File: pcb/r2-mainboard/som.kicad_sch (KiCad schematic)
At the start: 14 parts, among them J21 MICRO_SD(TFC-WPAPR-08), J26 BTH-060-01-L-D-A-K-TR, J27 BTH-060-01-L-D-A-K-TR, X2 PCM-071

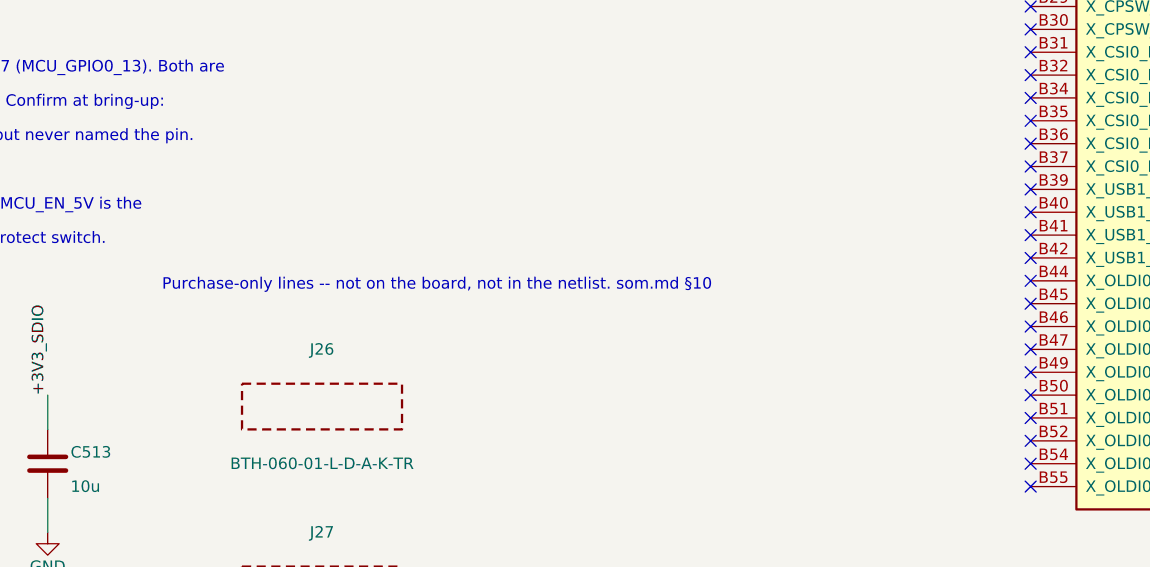
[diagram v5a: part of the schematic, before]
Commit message: R2: make the board arrive with the connectors already soldered
The question "why are they not on the board?" found a real hole, and my
previous commit had only half-fixed it. Making J26/J27 purchase-only put
the parts on the order and left the board unassemblable, because a part
that is not on the board is not in the position file either.

A CPL has one row per reference. X2 alone produces a single placement at a
single centroid, for a footprint that two separate parts occupy 22.4 mm
apart and 4.8 mm staggered -- there is no part covering all 240 pads. And
JLCPCB rejects a CPL designator with no BOM line, which X2 is. A board
ordered that way comes back with 240 bare pads.

So the two jobs are split. The pads stay under X2, which is now marked
exclude_from_pos_files. J26/J27 get r2:BTH-060-01-L-D-A-K_AssemblyOnly --
a body outline with no pads -- so each receptacle gets its own CPL row and
its own BOM match against C3646540. The assembler places a real part at
each real centroid; the paste and copper it lands on come from X2, which
they never need to know about.

Nothing in KiCad ties the three footprints together, so the relationship is
asserted rather than remembered: check_pcb_connectors.py requires
J26 = X2 + (-11.200, +2.400) and J27 = X2 + (+11.200, -2.400), plus same
side, same rotation, no pads on the markers, and the exclude_from_pos_files
split intact. Tested against three synthetic boards -- passes the good one,
catches a 2 mm nudge and a missing exclusion. That is a stronger guarantee
than the single footprint gave, which was unbreakable but also unverifiable.

517 nets before and after, ERC unchanged at 32. Two things still to confirm
with JLCPCB before the first order, both in som.md 10.0: whether their DFM
review accepts a no-pad designator, and the CPL rotation convention for
these connectors.

Co-Authored-By: Claude Opus 5 <noreply@anthropic.com>
Claude-Session: https://claude.ai/code/session_01MnesETWABbVdbcVnCKfKVs
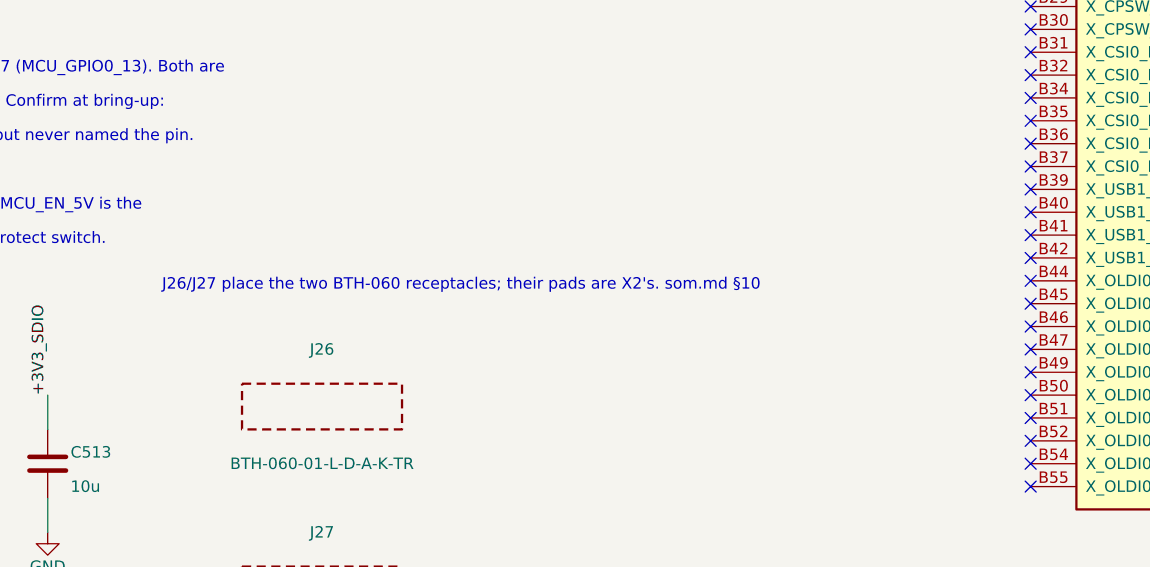
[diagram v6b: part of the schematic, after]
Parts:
- J26: footprint (none) -> r2:BTH-060-01-L-D-A-K_AssemblyOnly; BOM Comments Board-side receptacle for the PCM-071, 2 per board. Soldere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 -> Board-side receptacle for the PCM-071, 2 per board, SOLDERE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
- J27: footprint (none) -> r2:BTH-060-01-L-D-A-K_AssemblyOnly; BOM Comments The second of the two. See J26. -> The second of the two. Place at X2 + (+11.200, -2.400). See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
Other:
- note added: "J26/J27 place the two BTH-060 receptacles; their pads are X2's. som.md §10"
- note removed: "Purchase-only lines -- not on the board, not in the netlist. som.md §10"
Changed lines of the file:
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@@
 		)
 	)
-	(text "Purchase-only lines -- not on the board, not in the netlist. som.md §10"
+	(text "J26/J27 place the two BTH-060 receptacles; their pads are X2's. som.md §10"
 		(exclude_from_sim no)
 		(at 218.44 190.5 0)
@@
 		(exclude_from_sim no)
 		(in_bom yes)
-		(on_board no)
+		(on_board yes)
 		(dnp no)
 		(property "Reference" "J26"
@@
 			)
 		)
-		(property "Footprint" ""
+		(property "Footprint" "r2:BTH-060-01-L-D-A-K_AssemblyOnly"
 			(at 236.22 203.2 0)
 			(hide yes)
@@
 			)
 		)
-		(property "BOM Comments" "Board-side receptacle for the PCM-071, 2 per board. Soldered to r2:PCM-071_2xBTH-060-01-L-D-A-K, which carries both patterns in one footprint -- so this symbol is on_board=no and exists only to put the part on the order. LCSC stock was 60 on 2026-08-20; C3644612 is the same connector without the -K option. som.md section 10."
+		(property "BOM Comments" "Board-side receptacle for the PCM-071, 2 per board, SOLDERED BY THE ASSEMBLER. Its pads are in r2:PCM-071_2xBTH-060-01-L-D-A-K under X2; this reference carries the CPL row and the BOM match, and its own footprint has no pads. Place at X2 + (-11.200, +2.400) -- checked by tools/check_pcb_connectors.py. LCSC stock was 60 on 2026-08-20; C3644612 is the same connector without the -K option. som.md section 10."
 			(at 236.22 203.2 0)
 			(hide yes)
@@
 		(exclude_from_sim no)
 		(in_bom yes)
-		(on_board no)
+		(on_board yes)
 		(dnp no)
 		(property "Reference" "J27"
@@
 			)
 		)
-		(property "Footprint" ""
+		(property "Footprint" "r2:BTH-060-01-L-D-A-K_AssemblyOnly"
 			(at 236.22 223.52 0)
 			(hide yes)
@@
 			)
 		)
-		(property "BOM Comments" "The second of the two. See J26."
+		(property "BOM Comments" "The second of the two. Place at X2 + (+11.200, -2.400). See J26."
 			(at 236.22 223.52 0)
 			(hide yes)

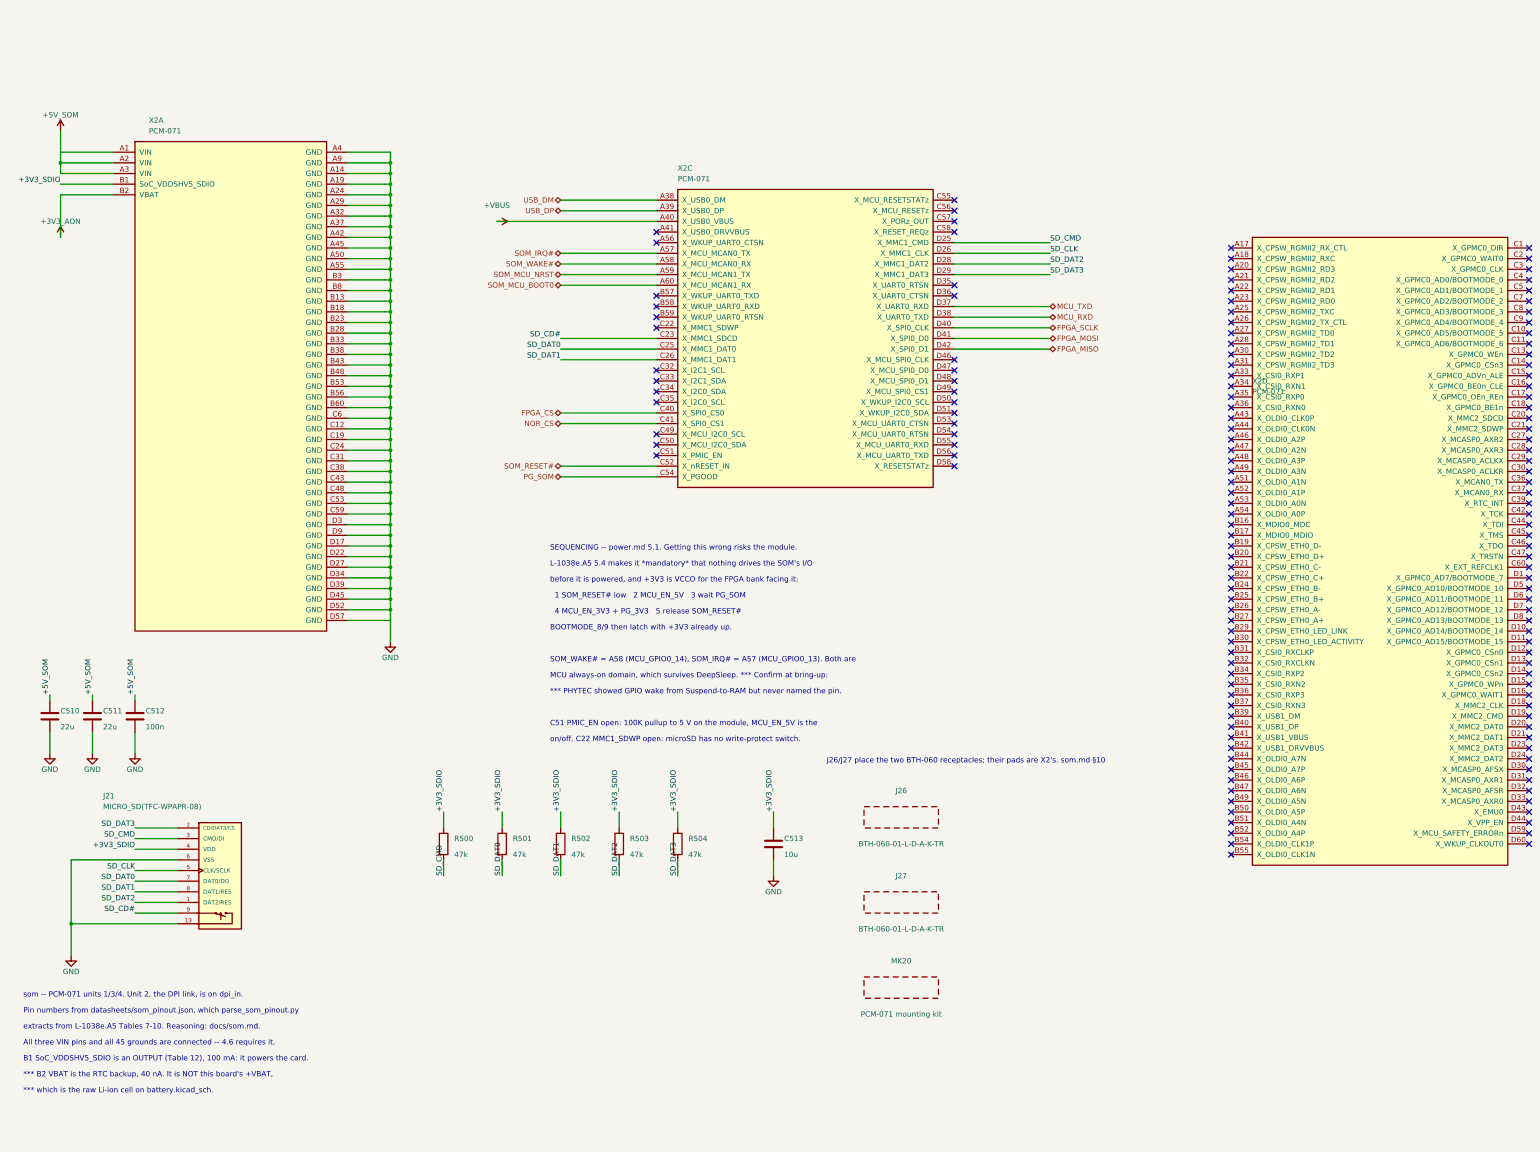
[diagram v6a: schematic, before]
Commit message: R2: the SoM is now two connectors, which is what the board has
The owner's call, and the right one: "I would rather have the two BTH
connectors and connect all signals/lines etc. to those two instead of the
A,B,... split. Then routing it later would also make more sense for me."
Clever loses to clear -- and the clever version could not be assembled
anyway, because a position file has one row per reference and there is no
single part covering 240 pads.

J26 carries the module's A and B columns, J27 its C and D, 120 pins each.
X2 survives as the module: outline and the two M2.5 holes, no pads, no
nets, excluded from the position file because it is fitted by hand. Three
footprints replace the one. Six unit boxes on som instead of three, two on
dpi_in instead of one; the root hierarchy is untouched.

What made this safe is that it is a repartition, not a renumber. Pin
numbers stay A1-A60 / B1-B60 / C1-C60 / D1-D60 exactly as L-1038e.A5
Tables 7-10 print them -- not Samtec's 1-120 alternating numbering -- and
the footprints name their pads the same way. Names, numbers and electrical
types are untouched; only which symbol a pin belongs to changes.

The acceptance test was exact: the netlist must be identical except every
X2.<pin> becomes J26.<pin> or J27.<pin> by row. It is -- 517 nets, 270
named nets with identical membership, 247 unconnected pins. ERC unchanged
at 32. Both sheets rendered and checked; two text collisions found that way
and fixed by deriving ref/val offsets from each box's own height.

check_pcb_connectors.py keeps the geometry guarantee the single footprint
used to give structurally, and now verifies it instead: J26 = X2 +
(-11.200, -2.400), J27 = X2 + (+11.200, +2.400), same side, same rotation,
122 pads each against the module's 2.

Two bugs fixed on the way, neither about the restructure. gen_som.py could
not find som_pinout.json -- it hardcoded datasheets/<name>, which broke in
the 2026-08-19 reorganisation; 058e9b9 fixed three tools and missed this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
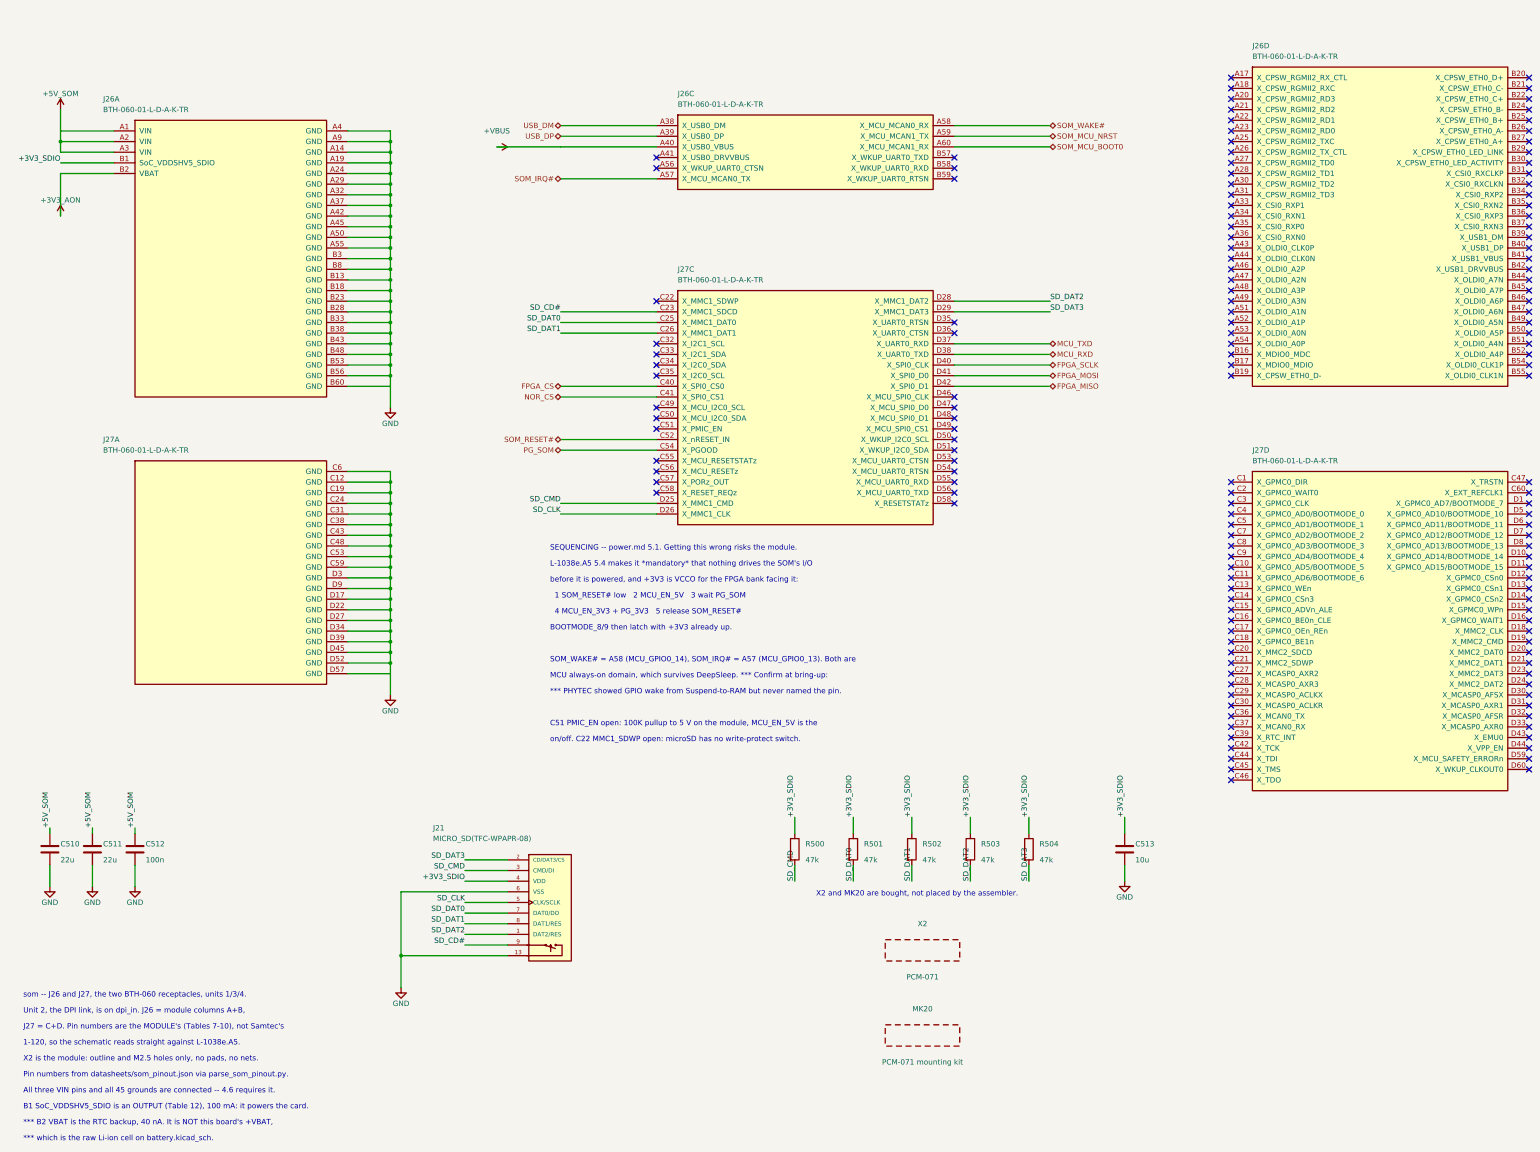
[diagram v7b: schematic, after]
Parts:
- removed J26, J27: BTH-060-01-L-D-A-K-TR, r2:BTH-060-01-L-D-A-K_AssemblyOnly, symbol r2:BOM_ITEM
- removed X2: PCM-071, r2:PCM-071_2xBTH-060-01-L-D-A-K, symbol r2:PCM-071
- added J26: BTH-060-01-L-D-A-K-TR, r2:BTH-060-01-L-D-A-K_AB, symbol r2:BTH-060_AB
- added J27: BTH-060-01-L-D-A-K-TR, r2:BTH-060-01-L-D-A-K_CD, symbol r2:BTH-060_CD
- added X2: PCM-071, r2:PCM-071_Module, symbol r2:BOM_ITEM
- MK20: BOM Comments PHYTEC's own recommendation, L-1038e.A5 section 4.3. Not optional: the standoffs set the 5 mm stacking height the BTH-060 pair is specified for, so without them the connector solder joints carry the module's mechanical load. Holes are in the footprint at (2.8, 2.8) and (29.2, 40.2) relative to the module outline. -> PHYTEC's own recommendation, L-1038e.A5 section 4.3. Not optional: the standoffs set the 5 mm stacking height the BTH-060 pair is specified for, so without them the connector solder joints carry the module's mechanical load.
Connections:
- net +3V3_AON: now also J26.B2 (VBAT)
- net +3V3_SDIO: now also J26.B1 (SoC_VDDSHV5_SDIO)
- net +5V_SOM: now also J26.A1 (VIN), J26.A2 (VIN), J26.A3 (VIN)
- net +VBUS: now also J26.A40 (X_USB0_VBUS)
- net FPGA_CS: now also J27.C40 (X_SPI0_CS0)
- net FPGA_MISO: now also J27.D42 (X_SPI0_D1)
- net FPGA_MOSI: now also J27.D41 (X_SPI0_D0)
- net FPGA_SCLK: now also J27.D40 (X_SPI0_CLK)
- net GND: now also J26.A14 (GND), J26.A19 (GND), J26.A24 (GND), J26.A29 (GND), J26.A32 (GND), J26.A37 (GND), J26.A4 (GND), J26.A42 (GND), J26.A45 (GND), J26.A50 (GND), J26.A55 (GND), J26.A9 (GND), J26.B13 (GND), J26.B18 (GND), J26.B23 (GND), J26.B28 (GND), J26.B3 (GND), J26.B33 (GND), J26.B38 (GND), J26.B43 (GND), J26.B48 (GND), J26.B53 (GND), J26.B56 (GND), J26.B60 (GND), J26.B8 (GND), J27.C12 (GND), J27.C19 (GND), J27.C24 (GND), J27.C31 (GND), J27.C38 (GND), J27.C43 (GND), J27.C48 (GND), J27.C53 (GND), J27.C59 (GND), J27.C6 (GND), J27.D17 (GND), J27.D22 (GND), J27.D27 (GND), J27.D3 (GND), J27.D34 (GND), J27.D39 (GND), J27.D45 (GND), J27.D52 (GND), J27.D57 (GND), J27.D9 (GND)
- net MCU_RXD: now also J27.D38 (X_UART0_TXD)
- net MCU_TXD: now also J27.D37 (X_UART0_RXD)
- net NOR_CS: now also J27.C41 (X_SPI0_CS1)
- net PG_SOM: now also J27.C54 (X_PGOOD)
- net SD_CD#: now also J27.C23 (X_MMC1_SDCD)
- net SD_CLK: now also J27.D26 (X_MMC1_CLK)
- net SD_CMD: now also J27.D25 (X_MMC1_CMD)
- net SD_DAT0: now also J27.C25 (X_MMC1_DAT0)
- net SD_DAT1: now also J27.C26 (X_MMC1_DAT1)
- net SD_DAT2: now also J27.D28 (X_MMC1_DAT2)
- net SD_DAT3: now also J27.D29 (X_MMC1_DAT3)
- net SOM_IRQ#: now also J26.A57 (X_MCU_MCAN0_TX)
- net SOM_MCU_BOOT0: now also J26.A60 (X_MCU_MCAN1_RX)
- net SOM_MCU_NRST: now also J26.A59 (X_MCU_MCAN1_TX)
- net SOM_RESET#: now also J27.C52 (X_nRESET_IN)
- net SOM_WAKE#: now also J26.A58 (X_MCU_MCAN0_RX)
- net USB_DM: now also J26.A38 (X_USB0_DM)
- net USB_DP: now also J26.A39 (X_USB0_DP)
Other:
- note added: "1-120, so the schematic reads straight against L-1038e.A5."
- note added: "J27 = C+D. Pin numbers are the MODULE's (Tables 7-10), not Samtec's"
- note added: "Pin numbers from datasheets/som_pinout.json via parse_som_pinout.py."
- note added: "Unit 2, the DPI link, is on dpi_in. J26 = module columns A+B,"
- note added: "X2 and MK20 are bought, not placed by the assembler."
- note added: "X2 is the module: outline and M2.5 holes only, no pads, no nets."
- note added: "som -- J26 and J27, the two BTH-060 receptacles, units 1/3/4."
- note removed: "J26/J27 place the two BTH-060 receptacles; their pads are X2's. som.md §10"
- note removed: "Pin numbers from datasheets/som_pinout.json, which parse_som_pinout.py"
- note removed: "extracts from L-1038e.A5 Tables 7-10. Reasoning: docs/som.md."
- note removed: "som -- PCM-071 units 1/3/4. Unit 2, the DPI link, is on dpi_in."
